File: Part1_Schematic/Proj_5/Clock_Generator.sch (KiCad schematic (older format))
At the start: 5 parts

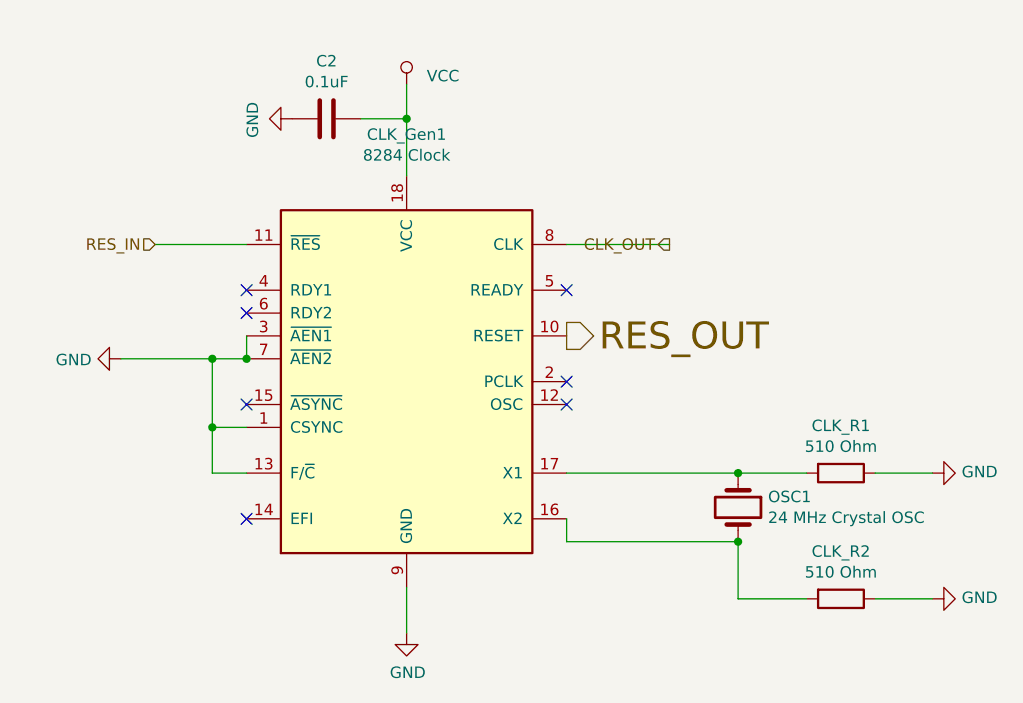
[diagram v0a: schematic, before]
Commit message: Addressing for 8279 and 8259
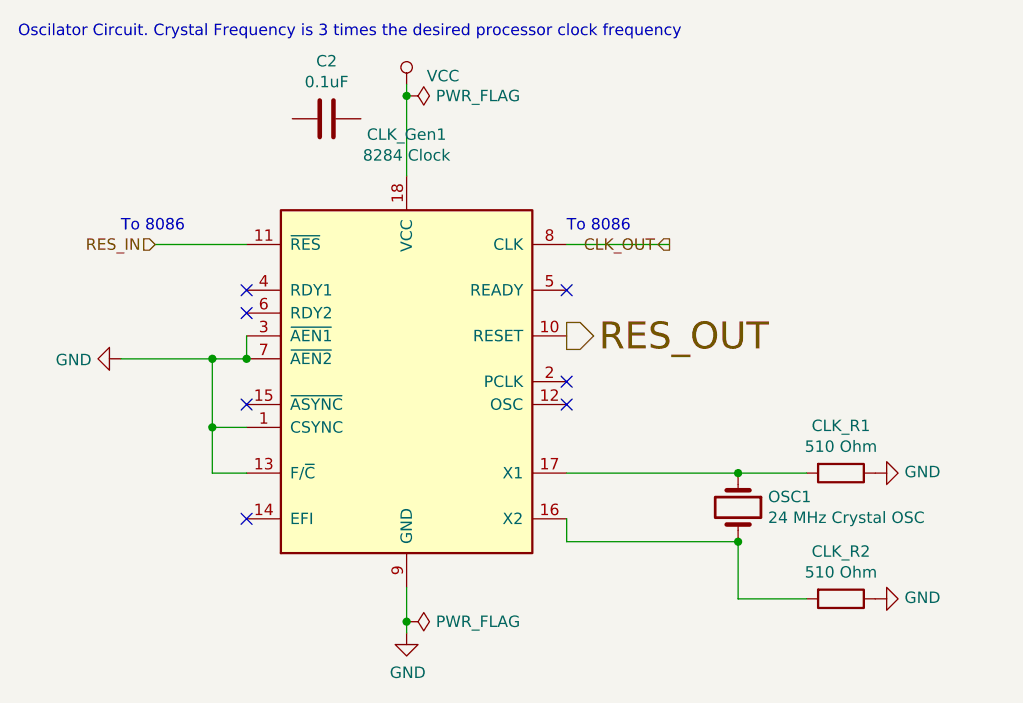
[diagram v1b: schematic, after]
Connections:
- net GND: no longer C2.2
- net VCC: no longer C2.1
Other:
- note added: "Oscilator Circuit. Crystal Frequency is 3 times the desired processor clock frequency"
- note added: "To 8086 \n"
- note added: "To 8086\n"
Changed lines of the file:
@@
 $Descr A4 11693 8268
 encoding utf-8
-Sheet 2 10
+Sheet 2 9
 Title ""
 Date ""
@@
 L power:GND #PWR?
 U 1 1 5EA0B827
-P 4800 2800
+P 4550 2800
 AR Path="/5EA0B827" Ref="#PWR?"  Part="1"
 AR Path="/5E9E2E0E/5EA0B827" Ref="#PWR0101"  Part="1"
-F 0 "#PWR0101" H 4800 2550 50  0001 C CNN
-F 1 "GND" V 4805 2672 50  0000 R CNN
-F 2 "" H 4800 2800 50  0001 C CNN
-F 3 "" H 4800 2800 50  0001 C CNN
-	1    4800 2800
+F 0 "#PWR0101" H 4550 2550 50  0001 C CNN
+F 1 "GND" V 4555 2672 50  0000 R CNN
+F 2 "" H 4550 2800 50  0001 C CNN
+F 3 "" H 4550 2800 50  0001 C CNN
+	1    4550 2800
 	0    -1   -1   0
 $EndComp
@@
 L power:GND #PWR?
 U 1 1 5EA0B82D
-P 4800 3350
+P 4550 3350
 AR Path="/5EA0B82D" Ref="#PWR?"  Part="1"
 AR Path="/5E9E2E0E/5EA0B82D" Ref="#PWR0102"  Part="1"
-F 0 "#PWR0102" H 4800 3100 50  0001 C CNN
-F 1 "GND" V 4805 3222 50  0000 R CNN
-F 2 "" H 4800 3350 50  0001 C CNN
-F 3 "" H 4800 3350 50  0001 C CNN
-	1    4800 3350
+F 0 "#PWR0102" H 4550 3100 50  0001 C CNN
+F 1 "GND" V 4555 3222 50  0000 R CNN
+F 2 "" H 4550 3350 50  0001 C CNN
+F 3 "" H 4550 3350 50  0001 C CNN
+	1    4550 3350
 	0    -1   -1   0
 $EndComp
@@
 	1    0    0    -1
 $EndComp
+Wire Wire Line
+	2500 1100 2500 1150
+$Comp
+L power:PWR_FLAG #FLG?
+U 1 1 5EA0B83A
+P 2500 1150
+AR Path="/5EA0B83A" Ref="#FLG?"  Part="1"
+AR Path="/5E9E2E0E/5EA0B83A" Ref="#FLG0101"  Part="1"
+F 0 "#FLG0101" H 2500 1225 50  0001 C CNN
+F 1 "PWR_FLAG" V 2500 1278 50  0000 L CNN
+F 2 "" H 2500 1150 50  0001 C CNN
+F 3 "~" H 2500 1150 50  0001 C CNN
+	1    2500 1150
+	0    1    1    0
+$EndComp
+Connection ~ 2500 1150
+Wire Wire Line
+	2500 1150 2500 1500
 $Comp
 L power:GND #PWR?
@@
 $EndComp
 Wire Wire Line
+	2500 3300 2500 3450
+$Comp
+L power:PWR_FLAG #FLG?
+U 1 1 5EA0B849
+P 2500 3450
+AR Path="/5EA0B849" Ref="#FLG?"  Part="1"
+AR Path="/5E9E2E0E/5EA0B849" Ref="#FLG0102"  Part="1"
+F 0 "#FLG0102" H 2500 3525 50  0001 C CNN
+F 1 "PWR_FLAG" V 2500 3578 50  0000 L CNN
+F 2 "" H 2500 3450 50  0001 C CNN
+F 3 "~" H 2500 3450 50  0001 C CNN
+	1    2500 3450
+	0    1    1    0
+$EndComp
+Connection ~ 2500 3450
+Wire Wire Line
+	2500 3450 2500 3500
+Wire Wire Line
 	3950 3100 3950 3350
 Connection ~ 3950 3100
+Text Notes 800  900  0    50   ~ 0
+Oscilator Circuit. Crystal Frequency is 3 times the desired processor clock frequency
 Wire Wire Line
 	1800 2200 1800 2300
@@
 Wire Wire Line
 	1800 1800 1400 1800
+Text Notes 1250 1750 0    50   ~ 0
+To 8086 \n
+Text Notes 3200 1750 0    50   ~ 0
+To 8086\n
 Wire Wire Line
 	3200 1800 3650 1800
@@
 Text HLabel 3200 2200 2    118  Output ~ 0
 RES_OUT
-$Comp
-L power:GND #PWR?
-U 1 1 5EADFD76
-P 2000 1250
-AR Path="/5EADFD76" Ref="#PWR?"  Part="1"
-AR Path="/5E9E2E0E/5EADFD76" Ref="#PWR03"  Part="1"
-F 0 "#PWR03" H 2000 1000 50  0001 C CNN
-F 1 "GND" H 2005 1077 50  0000 C CNN
-F 2 "" H 2000 1250 50  0001 C CNN
-F 3 "" H 2000 1250 50  0001 C CNN
-	1    2000 1250
-	0    1    1    0
-$EndComp
-Wire Wire Line
-	2300 1250 2500 1250
-Connection ~ 2500 1250
-Wire Wire Line
-	2500 1250 2500 1500
-Wire Wire Line
-	4550 2800 4800 2800
-Wire Wire Line
-	2500 1100 2500 1250
-Wire Wire Line
-	4550 3350 4800 3350
-Wire Wire Line
-	2500 3300 2500 3500
 $EndSCHEMATC
